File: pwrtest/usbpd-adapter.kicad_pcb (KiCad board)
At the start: 2 copper layers, 75.7 x 45.6 mm, 93 parts, among them J1 Conn_01x04, J2 Conn_01x04, J3 USB_C_Receptacle_USB2.0_16P, J5 Screw_Terminal_01x03, Q1 BC857, Q2 BC857, Q3 BC857, Q7 BC847, Q8 BC847, U1 AP63205WU, U11 TL431, U12 TL431, U2 L7812, U4 TPS5430DDA, U5 L7905, U6 TL431DBZ, U7 TL431DBZ, U8 TL431DBZ, U9 CH224K

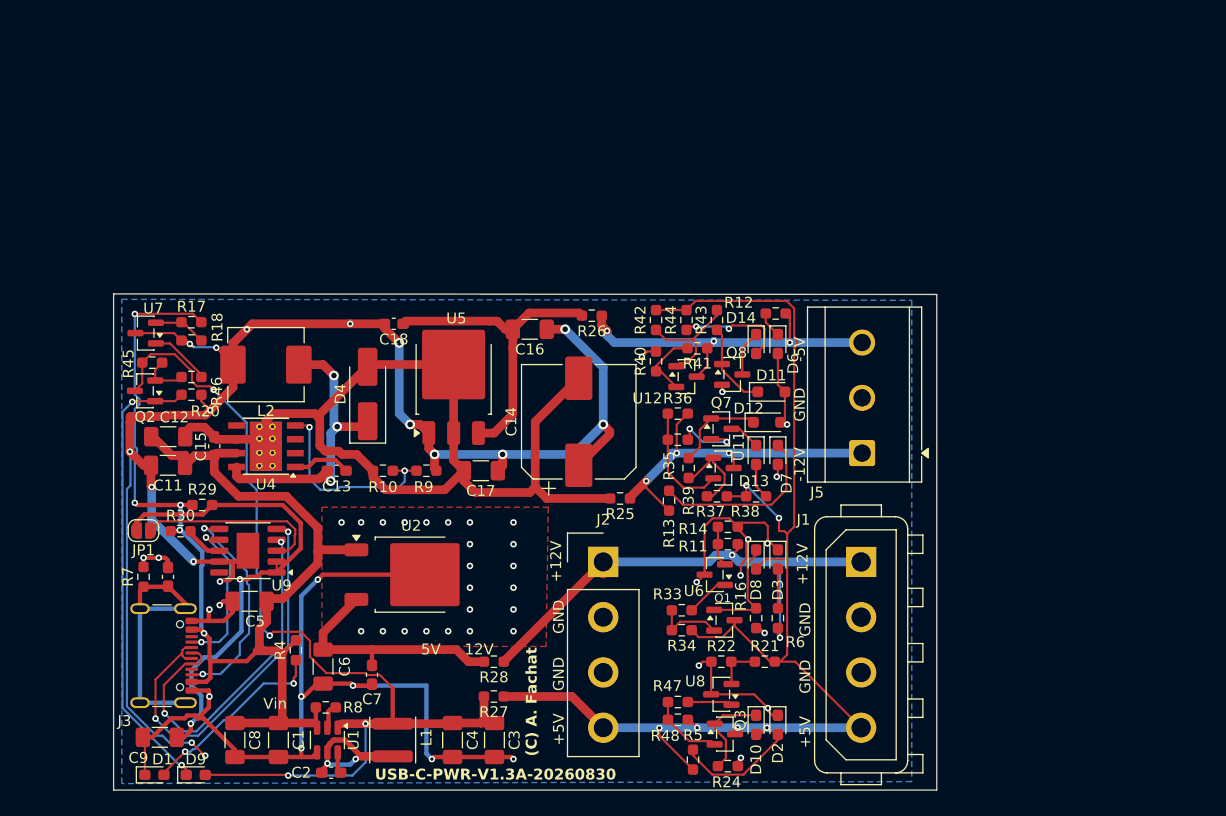
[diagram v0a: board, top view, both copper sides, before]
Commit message: add 3.3V and 9V to usb pwr
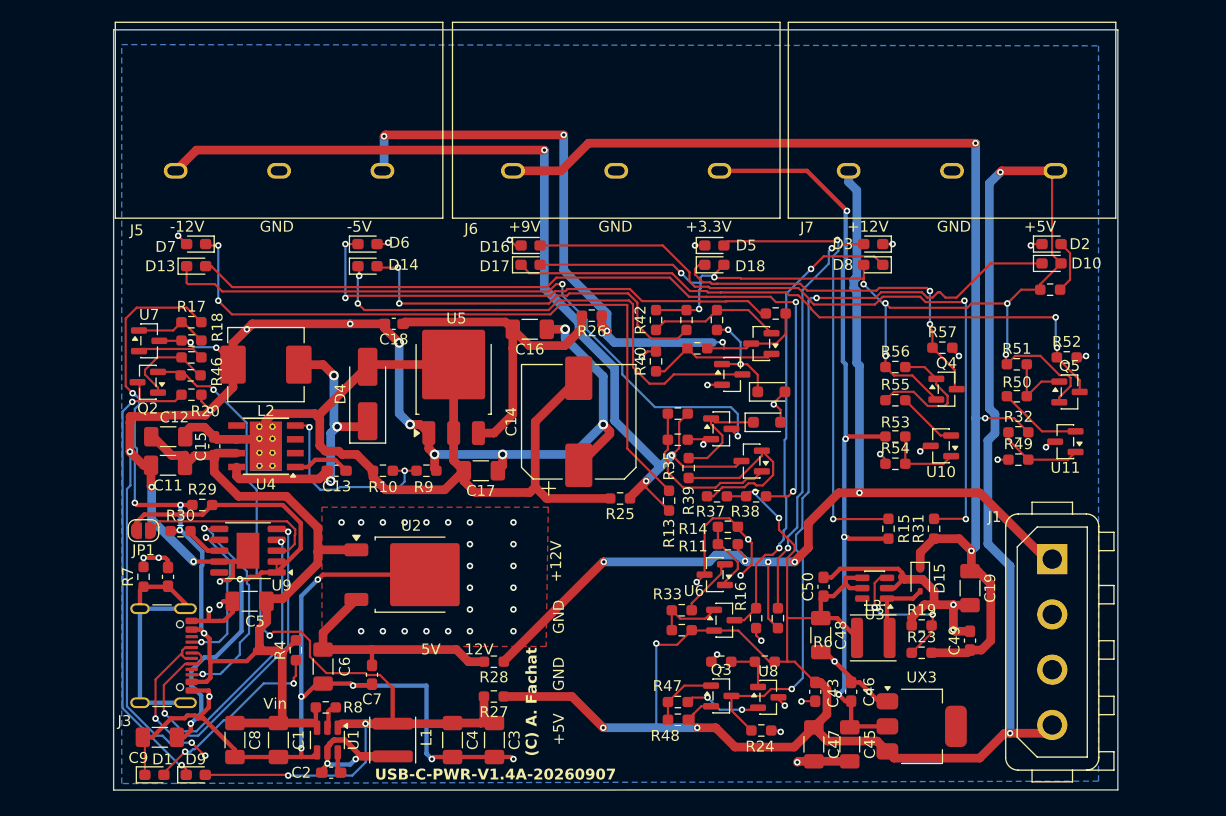
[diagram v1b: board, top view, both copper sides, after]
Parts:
- removed J2: Conn_01x04, Connector_Samtec_HPM_THT:Samtec_HPM-04-05-x-S_Straight_1x04_Pitch5.08mm
- added C19: 22u, Capacitor_SMD:C_1206_3216Metric_Pad1.33x1.80mm_HandSolder, F.Cu at (164.0, 82.0)
- added C43: 100n, Capacitor_SMD:C_0603_1608Metric_Pad1.08x0.95mm_HandSolder, F.Cu at (149.7, 91.6)
- added C45: 22u, Capacitor_SMD:C_1206_3216Metric_Pad1.33x1.80mm_HandSolder, F.Cu at (152.9, 96.4)
- added C46: 100n, Capacitor_SMD:C_0603_1608Metric_Pad1.08x0.95mm_HandSolder, F.Cu at (153.0, 91.6)
- added C47: 22u, Capacitor_SMD:C_1206_3216Metric_Pad1.33x1.80mm_HandSolder, F.Cu at (149.6, 96.4)
- added C48: 22u, Capacitor_SMD:C_1206_3216Metric_Pad1.33x1.80mm_HandSolder, F.Cu at (150.2, 86.4)
- added C49: 100n, Capacitor_SMD:C_0603_1608Metric_Pad1.08x0.95mm_HandSolder, F.Cu at (164.0, 86.9)
- added C50: 100n, Capacitor_SMD:C_0603_1608Metric_Pad1.08x0.95mm_HandSolder, F.Cu at (150.5, 81.9)
- added D15: 1N5819WS, Diode_SMD:D_SOD-323, F.Cu at (159.4, 81.3)
- added D16: LED, Diode_SMD:D_0603_1608Metric_Pad1.05x0.95mm_HandSolder, F.Cu at (123.6, 50.5)
- added D17: LED, Diode_SMD:D_0603_1608Metric_Pad1.05x0.95mm_HandSolder, F.Cu at (123.6, 52.3)
- added D18: LED, Diode_SMD:D_0603_1608Metric_Pad1.05x0.95mm_HandSolder, F.Cu at (140.5, 52.3)
- added D5: LED, Diode_SMD:D_0603_1608Metric_Pad1.05x0.95mm_HandSolder, F.Cu at (140.5, 50.5)
- added J6: Screw_Terminal_01x03, TermBlock:TermBlock HB9500-3P, F.Cu at (131.4, 43.7)
- added J7: Screw_Terminal_01x03, TermBlock:TermBlock HB9500-3P, F.Cu at (162.3, 43.7)
- added L3: 4.7uH, Inductor_SMD:L_APV_ANR4030, F.Cu at (155.1, 86.6)
- added Q4: BC857, Package_TO_SOT_SMD:SOT-23, F.Cu at (161.8, 63.8)
- added Q5: BC857, Package_TO_SOT_SMD:SOT-23, F.Cu at (173.1, 64.0)
- added R15: 68, Resistor_SMD:R_0603_1608Metric_Pad0.98x0.95mm_HandSolder, F.Cu at (156.5, 76.6)
- added R19: 2k3, Resistor_SMD:R_0603_1608Metric_Pad0.98x0.95mm_HandSolder, F.Cu at (159.5, 85.5)
- added R23: 33k, Resistor_SMD:R_0603_1608Metric_Pad0.98x0.95mm_HandSolder, F.Cu at (159.5, 88.0)
- added R31: 680, Resistor_SMD:R_0603_1608Metric_Pad0.98x0.95mm_HandSolder, F.Cu at (160.7, 76.6)
- added R32: 24k, Resistor_SMD:R_0603_1608Metric_Pad0.98x0.95mm_HandSolder, F.Cu at (168.4, 67.7)
- added R49: 10k, Resistor_SMD:R_0603_1608Metric_Pad0.98x0.95mm_HandSolder, F.Cu at (168.4, 70.2)
- added R50: 2k2, Resistor_SMD:R_0603_1608Metric_Pad0.98x0.95mm_HandSolder, F.Cu at (168.3, 64.4)
- added R51: 2k2, Resistor_SMD:R_0603_1608Metric_Pad0.98x0.95mm_HandSolder, F.Cu at (168.3, 61.5)
- added R52: 680, Resistor_SMD:R_0603_1608Metric_Pad0.98x0.95mm_HandSolder, F.Cu at (172.8, 60.8)
- added R53: 4k, Resistor_SMD:R_0603_1608Metric_Pad0.98x0.95mm_HandSolder, F.Cu at (157.1, 68.1)
- added R54: 10k, Resistor_SMD:R_0603_1608Metric_Pad0.98x0.95mm_HandSolder, F.Cu at (157.1, 70.6)
- added R55: 2k2, Resistor_SMD:R_0603_1608Metric_Pad0.98x0.95mm_HandSolder, F.Cu at (157.1, 64.8)
- added R56: 2k2, Resistor_SMD:R_0603_1608Metric_Pad0.98x0.95mm_HandSolder, F.Cu at (157.1, 61.7)
- added R57: 680, Resistor_SMD:R_0603_1608Metric_Pad0.98x0.95mm_HandSolder, F.Cu at (161.4, 59.9)
- added U10: TL431DBZ, Package_TO_SOT_SMD:SOT-23, F.Cu at (161.3, 69.0)
- added U13: TL431DBZ, Package_TO_SOT_SMD:SOT-23, F.Cu at (144.8, 59.6)
- added U3: MT3608, Package_TO_SOT_SMD:SOT-23-6, F.Cu at (155.2, 82.0)
- added UX3: LDI1117, Package_TO_SOT_SMD:SOT-223, F.Cu at (159.5, 94.7)
- J5: footprint TerminalBlock_CUI:TerminalBlock_CUI_TB007-508-03_1x03_P5.08mm_Horizontal -> TermBlock:TermBlock HB9500-3P
- U11, U12: value TL431 -> TL431DBZ
- moved J5 59.5 mm to (100.5, 43.7), turned to 180 degrees
- moved D7 56.9 mm to (92.8, 50.4), turned to 180 degrees
- moved D13 54.3 mm to (92.8, 52.5), turned to 0 degrees
- moved R5 54.2 mm to (171.3, 54.6), turned to 180 degrees
- moved D2 50.8 mm to (171.4, 50.4), turned to 0 degrees
- moved D10 50.4 mm to (171.4, 52.2), turned to 0 degrees
- moved D6 38.8 mm to (108.6, 50.4), turned to 0 degrees
- moved D14 36.4 mm to (108.6, 52.5), turned to 0 degrees
- moved U11 31.5 mm to (172.7, 68.6), turned to 180 degrees
- moved D3 30.3 mm to (155.1, 50.4), turned to 180 degrees
- moved D8 29.1 mm to (155.1, 52.3), turned to 180 degrees
- moved J1 17.6 mm to (171.5, 79.4)
- moved U12 9.80 mm to (143.9, 70.4), turned to 180 degrees
- moved R24 4.50 mm to (144.8, 95.1)
- moved U8 4.32 mm to (145.4, 92.1), turned to 0 degrees
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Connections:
- Q1 pad 1: Net-(D8-K) -> Net-(Q1-B)
- Q1 pad 2: Net-(Q1-B) -> 5V
- Q1 pad 3: 5V -> Net-(D8-K)
- Q2 pad 1: Net-(D9-K) -> Net-(Q2-B)
- Q2 pad 2: Net-(Q2-B) -> 5VP
- Q2 pad 3: 5VP -> Net-(D9-K)
- Q3 pad 1: Net-(D10-K) -> Net-(Q3-B)
- Q3 pad 2: Net-(Q3-B) -> 5V
- Q3 pad 3: 5V -> Net-(D10-K)
- R35 pad 1: Net-(U11-REF) -> Net-(U12-REF)
- R36 pad 2: Net-(U11-REF) -> Net-(U12-REF)
- R37 pad 1: Net-(U11-K) -> Net-(U12-K)
- R39 pad 2: Net-(U11-K) -> Net-(U12-K)
- R40 pad 1: Net-(U12-REF) -> Net-(U13-REF)
- R41 pad 2: Net-(U12-REF) -> Net-(U13-REF)
- R42 pad 1: Net-(U12-K) -> Net-(U13-K)
- R43 pad 2: Net-(U12-K) -> Net-(U13-K)
- U11 pad 1: Net-(U11-K) -> Net-(U11-REF)
- U11 pad 2: Net-(U11-REF) -> Net-(U11-K)
- U11 pad 3: -12V -> GND
- U12 pad 1: Net-(U12-K) -> Net-(U12-REF)
- U12 pad 2: Net-(U12-REF) -> Net-(U12-K)
- U12 pad 3: -5V -> -12V
- U6 pad 1: Net-(U6-K) -> Net-(U6-REF)
- U6 pad 2: Net-(U6-REF) -> Net-(U6-K)
- U7 pad 1: Net-(U7-K) -> Net-(U7-REF)
- U7 pad 2: Net-(U7-REF) -> Net-(U7-K)
- U8 pad 1: Net-(U8-K) -> Net-(U8-REF)
- U8 pad 2: Net-(U8-REF) -> Net-(U8-K)
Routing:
- net 5V: track 122.2 -> 282.2 mm, vias 6 -> 15
- net 9V: track 0.00 -> 109.2 mm, vias 0 -> 3
- net 3.3V: track 0.00 -> 73.4 mm, vias 0 -> 4
- net Net-(D13-A): track 3.30 -> 76.5 mm, vias 0 -> 2
- net Net-(D16-A): track 0.00 -> 65.4 mm, vias 0 -> 2
- net Net-(D10-K): track 8.77 -> 70.3 mm, vias 0 -> 2
- net Net-(D13-K): track 2.89 -> 62.3 mm, vias 0 -> 2
- net Net-(D17-K): track 0.00 -> 59.0 mm, vias 0 -> 2
- net -12V: track 32.4 -> 88.8 mm
- net 12V: track 47.5 -> 99.8 mm, vias 2 -> 5
- net Net-(D7-K): track 16.3 -> 63.5 mm, vias 0 -> 2
- net Net-(D6-K): track 2.39 -> 46.0 mm, vias 0 -> 2
- net Net-(D14-K): track 4.20 -> 46.4 mm, vias 0 -> 2
- net Net-(D5-A): track 0.00 -> 41.6 mm, vias 0 -> 2
- net Net-(D3-A): track 3.61 -> 38.2 mm, vias 0 -> 2
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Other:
- board size 75.7 x 45.6 mm -> 92.3 x 69.9 mm
- board text added: "+3.3V"
- board text added: "+9V"
- board text added: "USB-C-PWR-V1.4A-20260907"
- board text removed: "USB-C-PWR-V1.3A-20260830"

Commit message: update usb-c pwr adapter with mounting holes
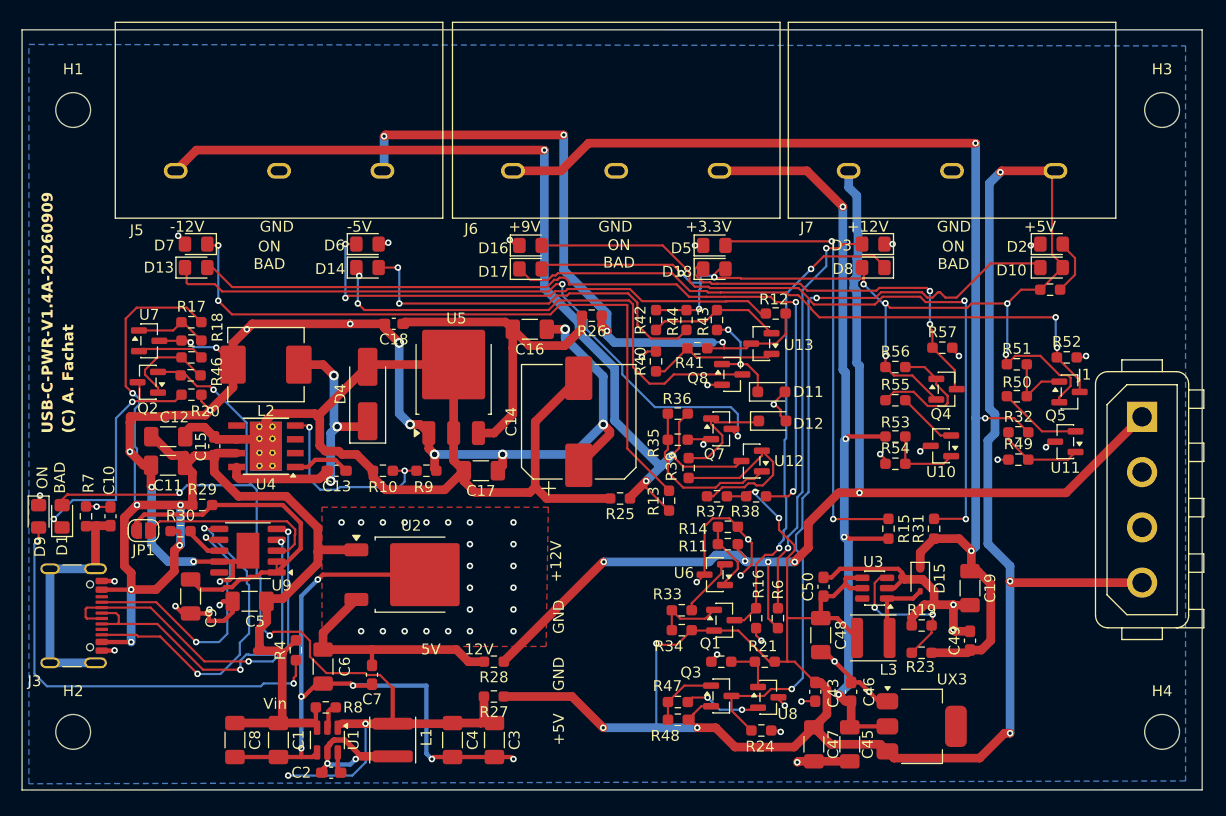
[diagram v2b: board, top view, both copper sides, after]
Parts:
- added H1: MountingHole, MountingHole:MountingHole_3.2mm_M3_DIN965, F.Cu at (81.5, 38.1)
- added H2: MountingHole, MountingHole:MountingHole_3.2mm_M3_DIN965, F.Cu at (81.5, 95.2)
- added H3: MountingHole, MountingHole:MountingHole_3.2mm_M3_DIN965, F.Cu at (181.6, 38.1)
- added H4: MountingHole, MountingHole:MountingHole_3.2mm_M3_DIN965, F.Cu at (181.6, 95.2)
- D1, D10, D13, D14, D16, D17, D18, D2, D3, D5, D6, D7, D8, D9: footprint Diode_SMD:D_0603_1608Metric_Pad1.05x0.95mm_HandSolder -> Diode_SMD:D_0805_2012Metric_Pad1.15x1.40mm_HandSolder
- moved D9 26.7 mm to (80.5, 75.4), turned to 90 degrees
- moved D1 26.0 mm to (78.4, 75.4), turned to -90 degrees
- moved J1 15.5 mm to (179.8, 66.3)
- moved C9 13.3 mm to (92.3, 82.8), turned to -90 degrees
- moved J3 9.05 mm to (80.5, 84.6)
- moved C10 7.67 mm to (85.0, 75.4)
- moved R7 7.67 mm to (82.7, 75.4)
- moved D12 0.51 mm to (145.8, 66.7)
- moved D10 0.38 mm to (171.4, 52.6)
- moved D17 0.38 mm to (123.6, 52.7)
- moved D18 0.38 mm to (140.5, 52.7)
- moved D8 0.25 mm to (155.1, 52.6)
- moved D13 0.13 mm to (92.8, 52.6)
- moved D14 0.13 mm to (108.6, 52.6)
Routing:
- net GND: track 321.6 -> 274.9 mm
- net Net-(D1-A): track 17.7 -> 40.4 mm
- net Net-(D9-K): track 43.8 -> 23.7 mm
- net Net-(JP1-B): track 46.1 -> 32.6 mm, vias 2 -> 0
- net 5VP: track 84.2 -> 95.3 mm, vias 4 -> 5
- net VBUS: track 119.1 -> 129.0 mm, vias 5 -> 6
- net Net-(J3-CC1): track 15.1 -> 24.8 mm
- net Net-(J3-CC2): track 20.4 -> 30.1 mm
- net 12V: track 99.8 -> 108.5 mm
- net 5V: track 282.2 -> 290.4 mm, vias 15 -> 16
- net Net-(U9-DM): track 37.4 -> 35.3 mm
- net Net-(U9-DP): track 33.3 -> 32.4 mm
- net Net-(J3-SHIELD): track 24.2 -> 23.3 mm
- net Net-(D5-A): track 41.6 -> 40.7 mm
- net Net-(D17-K): track 59.0 -> 59.8 mm
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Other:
- board size 92.3 x 69.9 mm -> 108.5 x 69.9 mm
- board text added: "C10"
- board text added: "D11"
- board text added: "D12"
- board text added: "ON BAD"
- board text added: "Q1"
- board text added: "Q7"
- board text added: "Q8"
- board text added: "R12"
- board text added: "R21"
- board text added: "R34"
- board text added: "R36"
- board text added: "R41"
- board text added: "R43"
- board text added: "R44"
- board text added: "U12"
- board text added: "U13"
- board text added: "USB-C-PWR-V1.4A-20260909"
- board text removed: "USB-C-PWR-V1.4A-20260907"

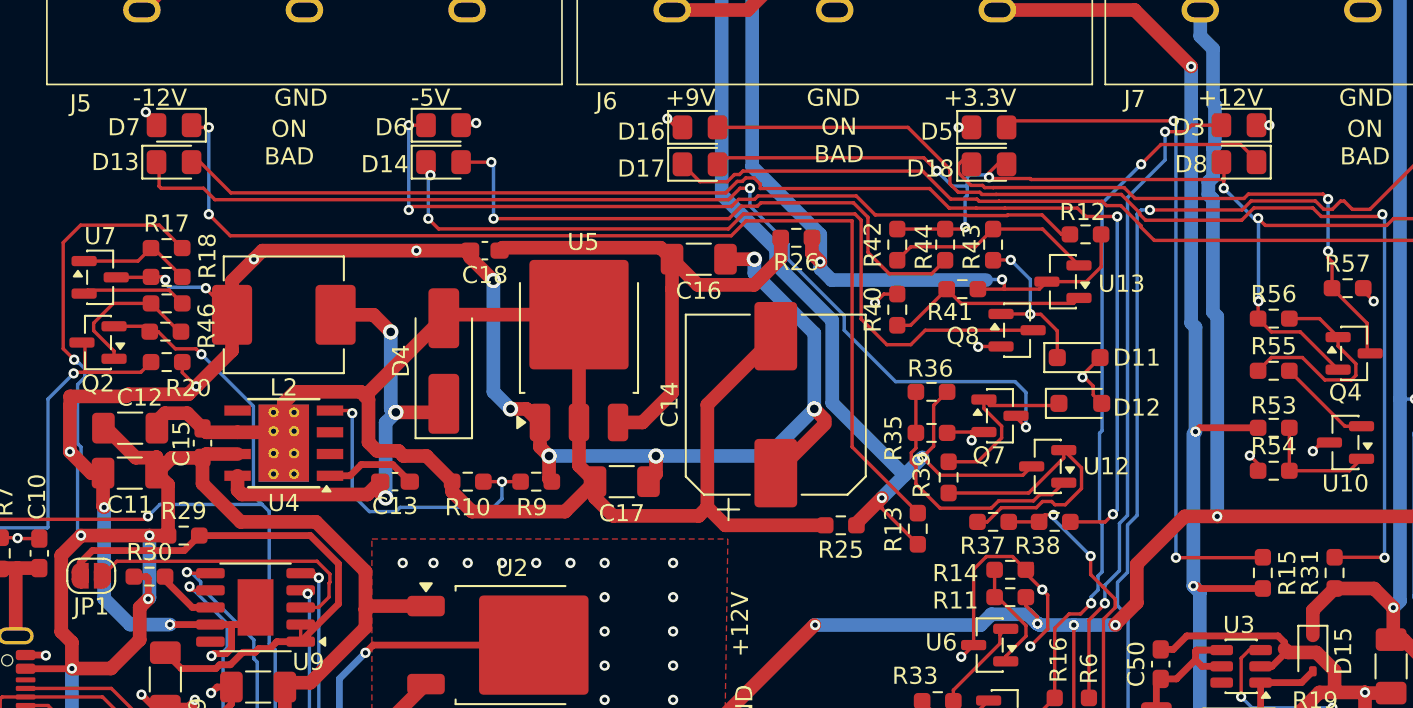
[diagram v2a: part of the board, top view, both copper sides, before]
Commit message: update pwr test pcb for production
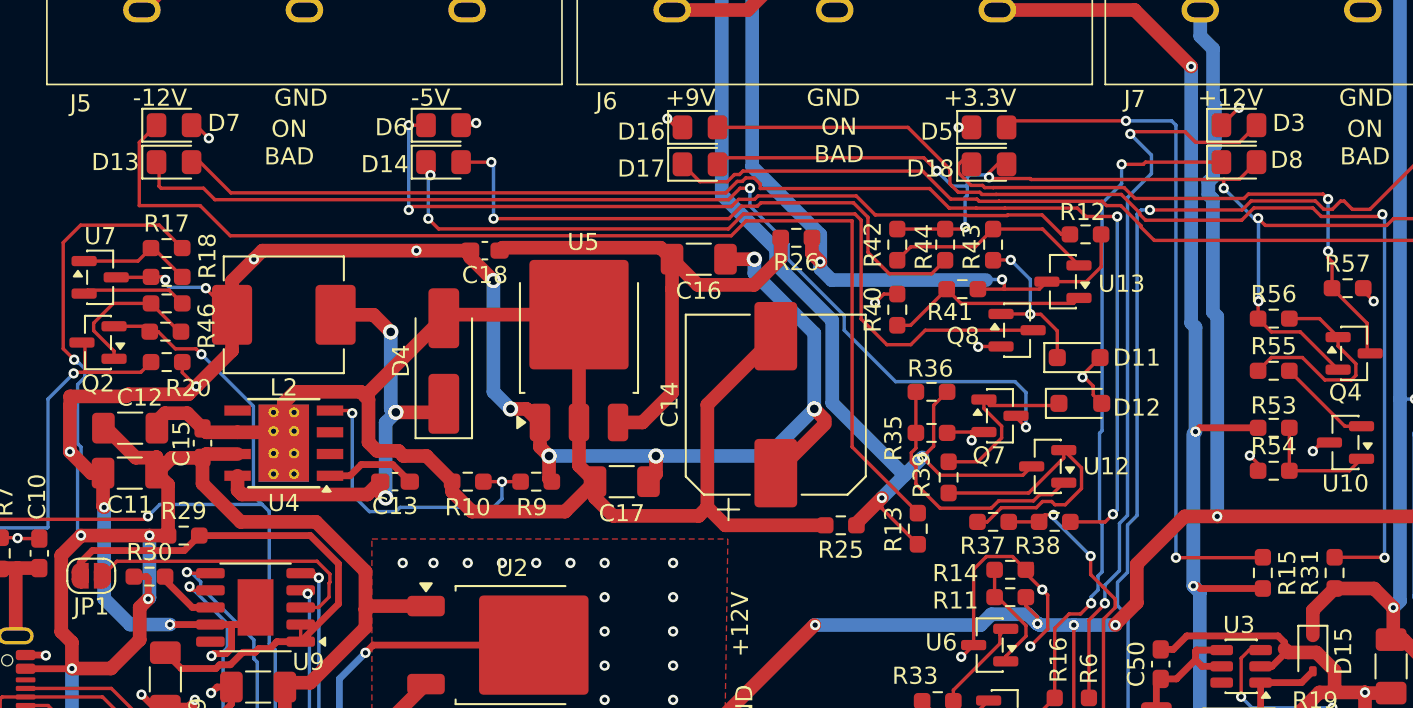
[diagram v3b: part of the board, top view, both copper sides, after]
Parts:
- turned D3 to 0 degrees
- turned D7 to 0 degrees
- turned D8 to 0 degrees
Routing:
- net Net-(D3-A): track 38.5 -> 43.1 mm
- net Net-(D7-K): track 63.5 -> 66.6 mm, vias 2 -> 0
- net Net-(D8-K): track 43.6 -> 41.6 mm
- net 5V: track 290.4 -> 291.5 mm
- net GND: track 274.9 -> 275.9 mm
